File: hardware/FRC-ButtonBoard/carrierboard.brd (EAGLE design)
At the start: 79.7 x 66 mm, 36 parts

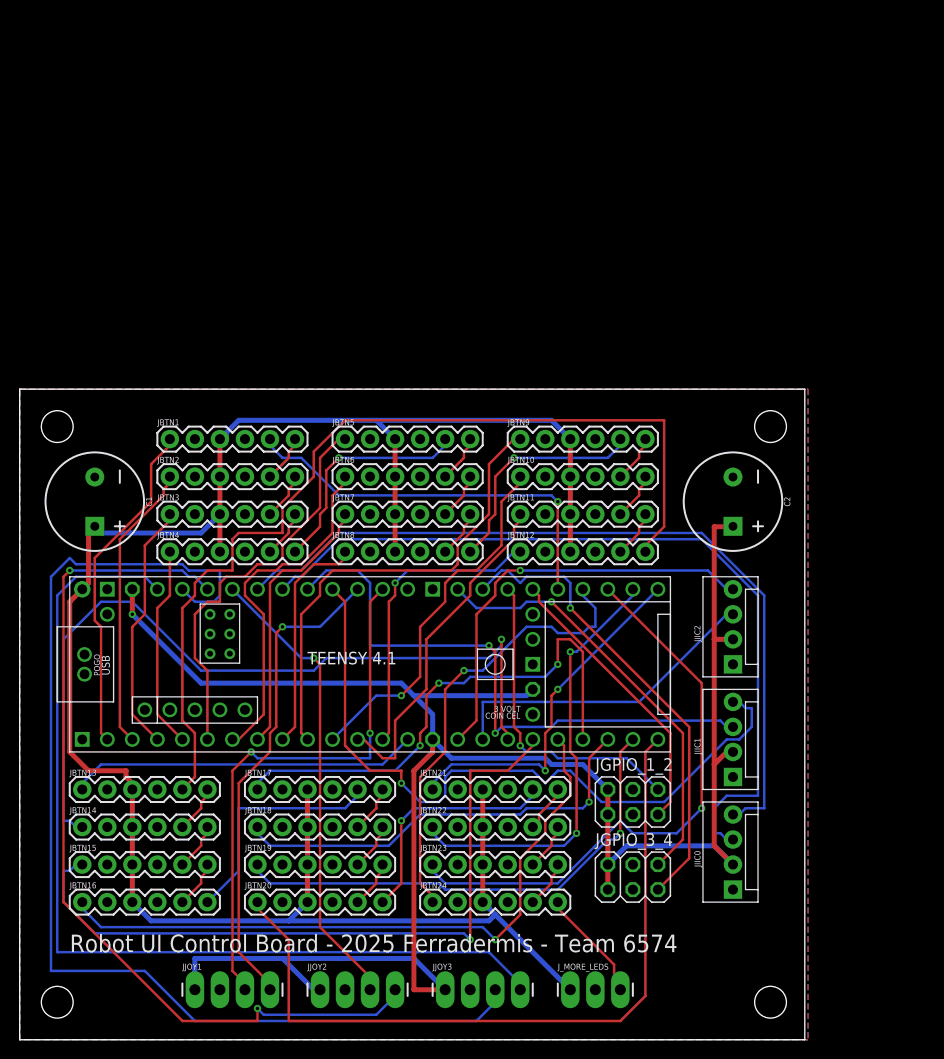
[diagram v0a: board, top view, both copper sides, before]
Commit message: switched connectors to JST HX
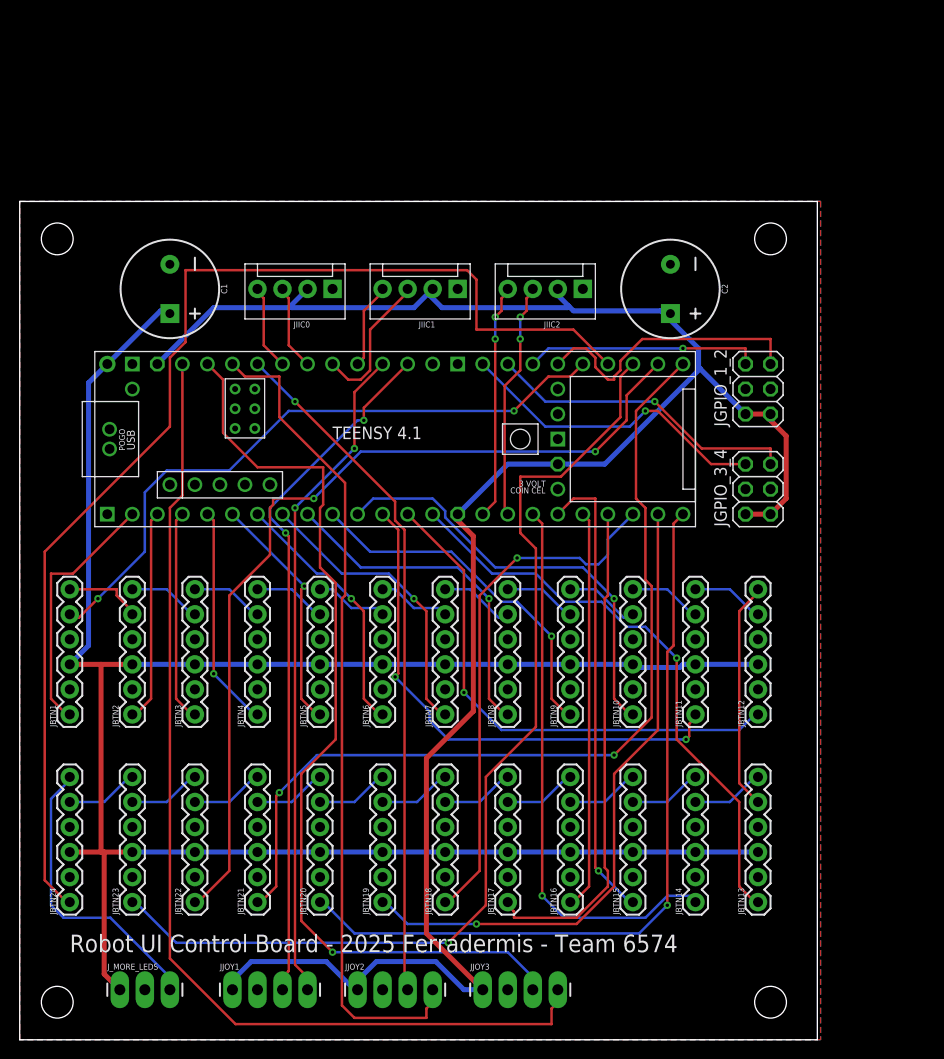
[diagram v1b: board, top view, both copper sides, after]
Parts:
- moved JIIC0 73.3 mm to (29.2, 73.7), turned to 180 degrees
- moved JBTN13 69.5 mm to (72.4, 11.4), turned to 90 degrees
- moved JBTN14 62.7 mm to (66.0, 11.4), turned to 90 degrees
- moved JIIC1 56.9 mm to (41.9, 73.7), turned to 180 degrees
- moved JBTN15 56.0 mm to (59.7, 11.4), turned to 90 degrees
- moved JBTN16 49.5 mm to (53.3, 11.4), turned to 90 degrees
- moved J_MORE_LEDS 45.7 mm to (7.62, 2.54)
- moved JGPIO_1_2 43.8 mm to (72.4, 63.5), turned to 90 degrees
- moved JGPIO_3_4 41.4 mm to (72.4, 53.3), turned to 90 degrees
- moved JIIC2 41.0 mm to (54.6, 73.7), turned to 180 degrees
- moved JBTN24 36.8 mm to (2.54, 11.4), turned to 90 degrees
- moved JBTN23 30.7 mm to (8.89, 11.4), turned to 90 degrees
- moved JBTN1 29.7 mm to (2.54, 30.5), turned to 90 degrees
- moved JBTN12 29.2 mm to (72.4, 30.5), turned to 90 degrees
- moved JBTN9 28.4 mm to (53.3, 30.5), turned to 90 degrees
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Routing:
- net BTN24: track 45.9 -> 121.1 mm, vias 1 -> 0
- net SDA0: track 82.7 -> 8.67 mm
- net SCL0: track 81.5 -> 8.67 mm
- net B13_DIN: track 96.0 -> 23.2 mm
- net SCL1: track 72.8 -> 8.67 mm, vias 1 -> 0
- net BTN21: track 36.3 -> 91.7 mm
- net BTN22: track 44.3 -> 90.6 mm
- net SDA1: track 60.2 -> 14.7 mm, vias 2 -> 0
- net BTN23: track 58.8 -> 104.0 mm
- net BTN16: track 67.9 -> 40.6 mm, vias 1 -> 0
- net BTN15: track 73.4 -> 47.2 mm
- net B1_DIN: track 41.1 -> 66.6 mm, vias 1 -> 2
- net BTN14: track 81.6 -> 56.8 mm
- net BTN13: track 35.5 -> 59.2 mm, vias 0 -> 1
- net JOY_Z: track 47.2 -> 69.8 mm
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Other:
- board size 79.7 x 66 mm -> 81 x 85.1 mm

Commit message: commit to more buttons
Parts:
- removed JGPIO_1_2, JGPIO_3_4: (no value), pinhead:2X03
- added C3: 0.1uF, SparkFun-Capacitors:CAP-PTH-SMALL-KIT
- added J1: USB_A_SMT_FEMALE, SparkFun-Connectors:USB-A-S-SILK-FEMALE
- added JBTN25, JBTN26, JBTN27, JBTN28: (no value), SparkFun-Connectors:1X06
- added JRST: (no value), pinhead:1X02
- added JUSB: USB_B_PTH, SparkFun-Connectors:USB-B-PTH
- added P1: J1B1211CCD, WIZnet:J1B1211CCD
- moved J_MORE_LEDS 99.8 mm to (74.9, 76.2), turned to 270 degrees
- moved JJOY1 98.1 mm to (54.6, 94.0), turned to 180 degrees
- moved JJOY2 88.1 mm to (54.6, 87.6), turned to 180 degrees
- moved JJOY3 79.4 mm to (54.6, 81.3), turned to 180 degrees
- moved JBTN14 63.5 mm to (2.54, 12.7)
- moved JBTN24 63.5 mm to (66.0, 12.7)
- moved JBTN15 50.8 mm to (8.89, 12.7)
- moved JBTN23 50.8 mm to (59.7, 12.7)
- moved JBTN16 38.1 mm to (15.2, 12.7)
- moved JBTN22 38.1 mm to (53.3, 12.7)
- moved JBTN17 25.4 mm to (21.6, 12.7)
- moved JBTN21 25.4 mm to (47.0, 12.7)
- moved JBTN13 21.3 mm to (78.7, 31.8)
- moved JBTN18 12.8 mm to (27.9, 12.7)
- moved JBTN20 12.8 mm to (40.6, 12.7)
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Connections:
- removed net GPIO1: JGPIO_1_2.5, U$1.38-A14/CS/IN1
- removed net GPIO2: JGPIO_1_2.6, U$1.39-A15/CS/OUT1A
- removed net GPIO3: JGPIO_3_4.5, U$1.40-A16/CS1
- removed net GPIO4: JGPIO_3_4.6, U$1.41-A17/MISO1
- new net B25_DIN: JBTN24.6, JBTN25.5
- new net B26_DIN: JBTN25.6, JBTN26.5
- new net B27_DIN: JBTN26.6, JBTN27.5
- new net B28_DIN: JBTN27.6, JBTN28.5
- new net BTN25: JBTN25.1, U$1.38-A14/CS/IN1
- new net BTN26: JBTN26.1, U$1.39-A15/CS/OUT1A
- new net BTN27: JBTN27.1, U$1.40-A16/CS1
- new net BTN28: JBTN28.1, U$1.41-A17/MISO1
- new net ETH_LED: P1.10, U$1.LED
- new net ETH_R+: P1.4, U$1.R+
- new net ETH_R-: P1.6, U$1.R-
- new net ETH_T+: P1.1, U$1.T+
- new net ETH_T-: P1.3, U$1.T-
- new net N$1: C3.2, P1.2, P1.5
- new net N$10: U$1.VUSB
- new net PROGRAM_RESET: JRST.1, U$1.PROGRAM
- new net USBH_D+: J1.D+, U$1.DP
- new net USBH_D-: J1.D-, U$1.DM
- new net USB_D+: JUSB.D+, U$1.D+
- new net USB_D-: JUSB.D-, U$1.D-
- net 3V3: no longer JGPIO_1_2.1, JGPIO_1_2.2, JGPIO_3_4.1, JGPIO_3_4.2
- net 5V: now also J1.VBUS, JBTN25.3, JBTN26.3, JBTN27.3, JBTN28.3, JUSB.VBUS, U$1.+5V
- net B_DOUT: now also JBTN28.6; no longer JBTN24.6
- net GND: now also C3.1, J1.GND, J1.SHLD1, J1.SHLD2, JBTN25.2, JBTN25.4, JBTN26.2, JBTN26.4, JBTN27.2, JBTN27.4, JBTN28.2, JBTN28.4, JRST.2, JUSB.GND, JUSB.SHLD1, JUSB.SHLD2, P1.13, P1.14, P1.8, P1.9, U$1.G; no longer JGPIO_1_2.3, JGPIO_1_2.4, JGPIO_3_4.3, JGPIO_3_4.4
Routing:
- net 5V: track 214.6 -> 322.7 mm, vias 0 -> 1
- net B14_DIN: track 7.40 -> 102.8 mm
- net 3V3: track 209.6 -> 117.4 mm, vias 0 -> 2
- net BTN26: track 0.00 -> 88.8 mm, vias 0 -> 2
- net USBH_D-: track 0.00 -> 71.9 mm, vias 0 -> 3
- net USBH_D+: track 0.00 -> 69.7 mm, vias 0 -> 1
- net BTN25: track 0.00 -> 69.2 mm, vias 0 -> 1
- net JOY_S2: track 106.1 -> 39.5 mm, vias 0 -> 2
- net ETH_LED: track 0.00 -> 62.3 mm
- net USB_D+: track 0.00 -> 62.1 mm
- net BTN24: track 121.1 -> 63.9 mm, vias 0 -> 2
- net JOY_S1: track 94.7 -> 44.9 mm, vias 1 -> 2
- net USB_D-: track 0.00 -> 47.0 mm, vias 0 -> 1
- net BTN23: track 104.0 -> 59.6 mm, vias 1 -> 0
- net B27_DIN: track 0.00 -> 44.1 mm
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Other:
- board size 81 x 85.1 mm -> 86 x 95.2 mm
